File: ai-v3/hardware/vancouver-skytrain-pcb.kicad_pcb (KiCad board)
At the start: 2 copper layers, 150 x 150 mm, 85 parts, among them SW1 TS-1187A-B-A-B, SW2 TS-1187A-B-A-B, SW3 TS-1187A-B-A-B, SW4 TS-1187A-B-A-B, U1 XIAO-RP2040-DIP

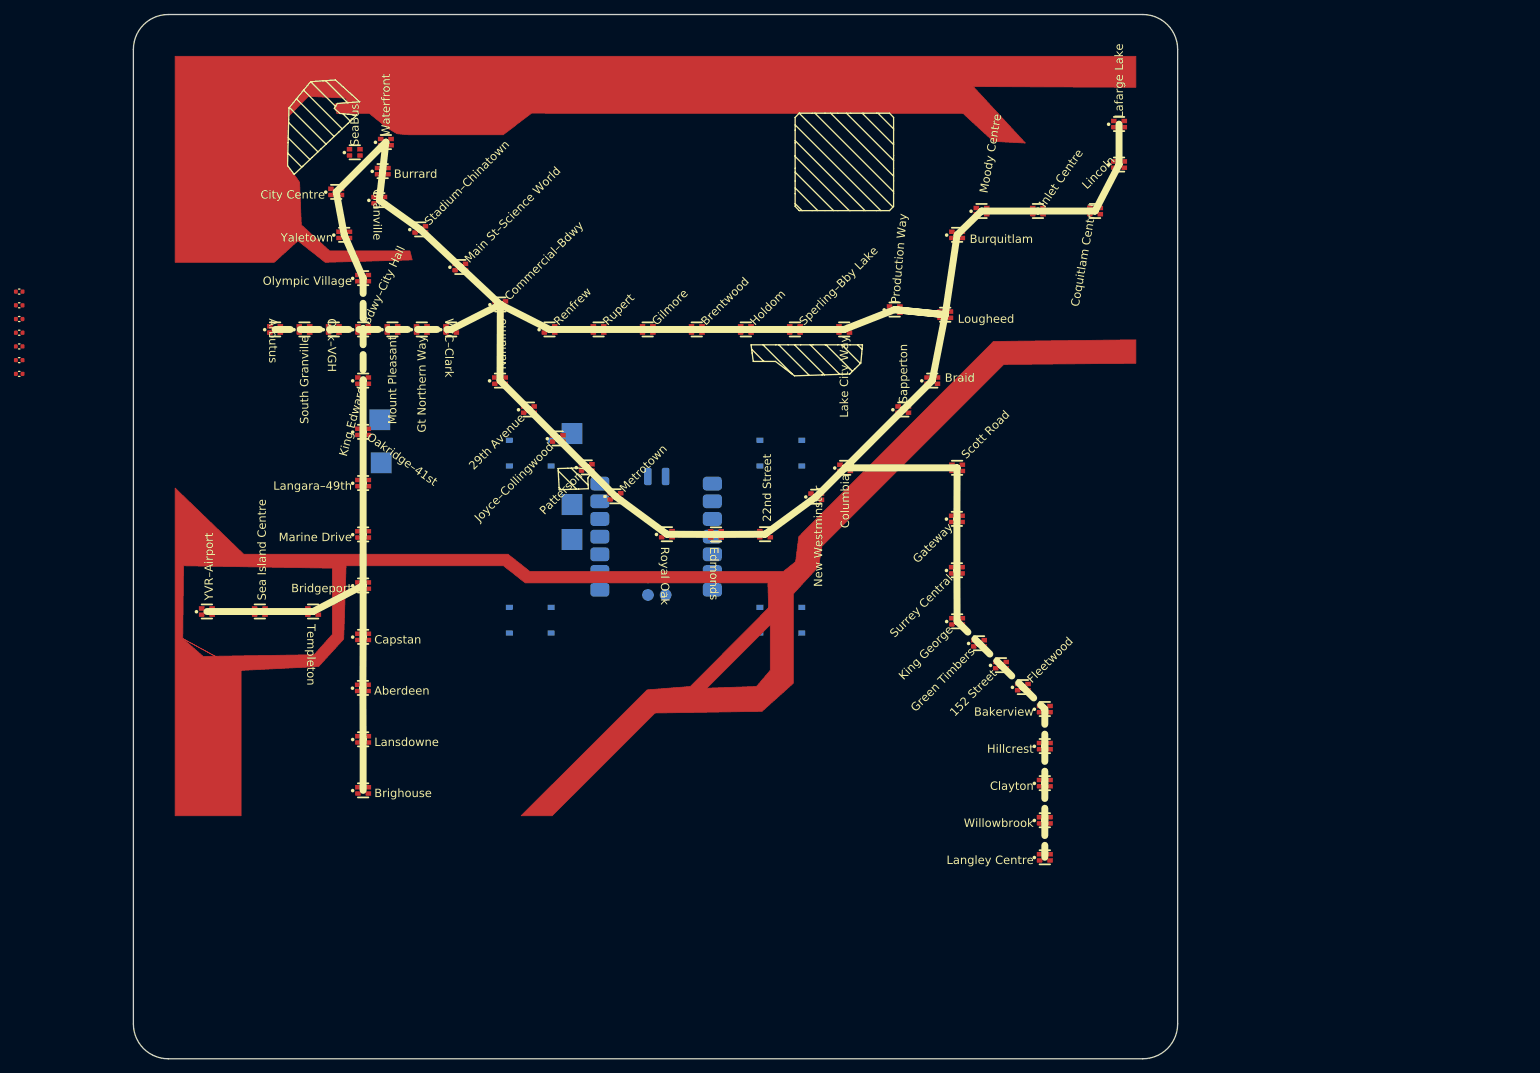
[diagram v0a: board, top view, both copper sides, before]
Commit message: ai-v3: design-review pass - west coast, Delta, wordmark, readable labels
Left edge now ends in water: build_geo.py carves the Point Grey tip out
of the traced land in the PDF's own 45-degree idiom (the source draws no
coastline west of Cambie; v2's look came from a wider frame, not from
data), and the frame extends below the page so Delta / the South Arm /
Boundary Bay fill the bottom third instead of blank soldermask.

Map furniture: exposed-copper VANCOUVER wordmark (v2 style), 49th
parallel dash-dot border with CANADA/USA, legend (existing / future /
SeaBus), SeaBus dotted ferry route. New "line" geo type and "copper"
annotations in export_art.

Labels: 0.15 mm stroke, 1.9 mm standoff from the LED, two-line wrapping
of long names (no more Bdwy/Bby abbreviations), leader hairlines for
stations with no clean spot beside the pad. auto_label rewritten to
score per station (check_fit.Context fast path, 10 s instead of hours),
prefer one angle per corridor, and check labels against their own route
segment beyond the standoff. Routes 1.5 mm; silk station rings, heavier
at interchanges (Columbia, Bridgeport, Production Way now flagged).

Co-Authored-By: Claude Fable 5.1 <noreply@anthropic.com>
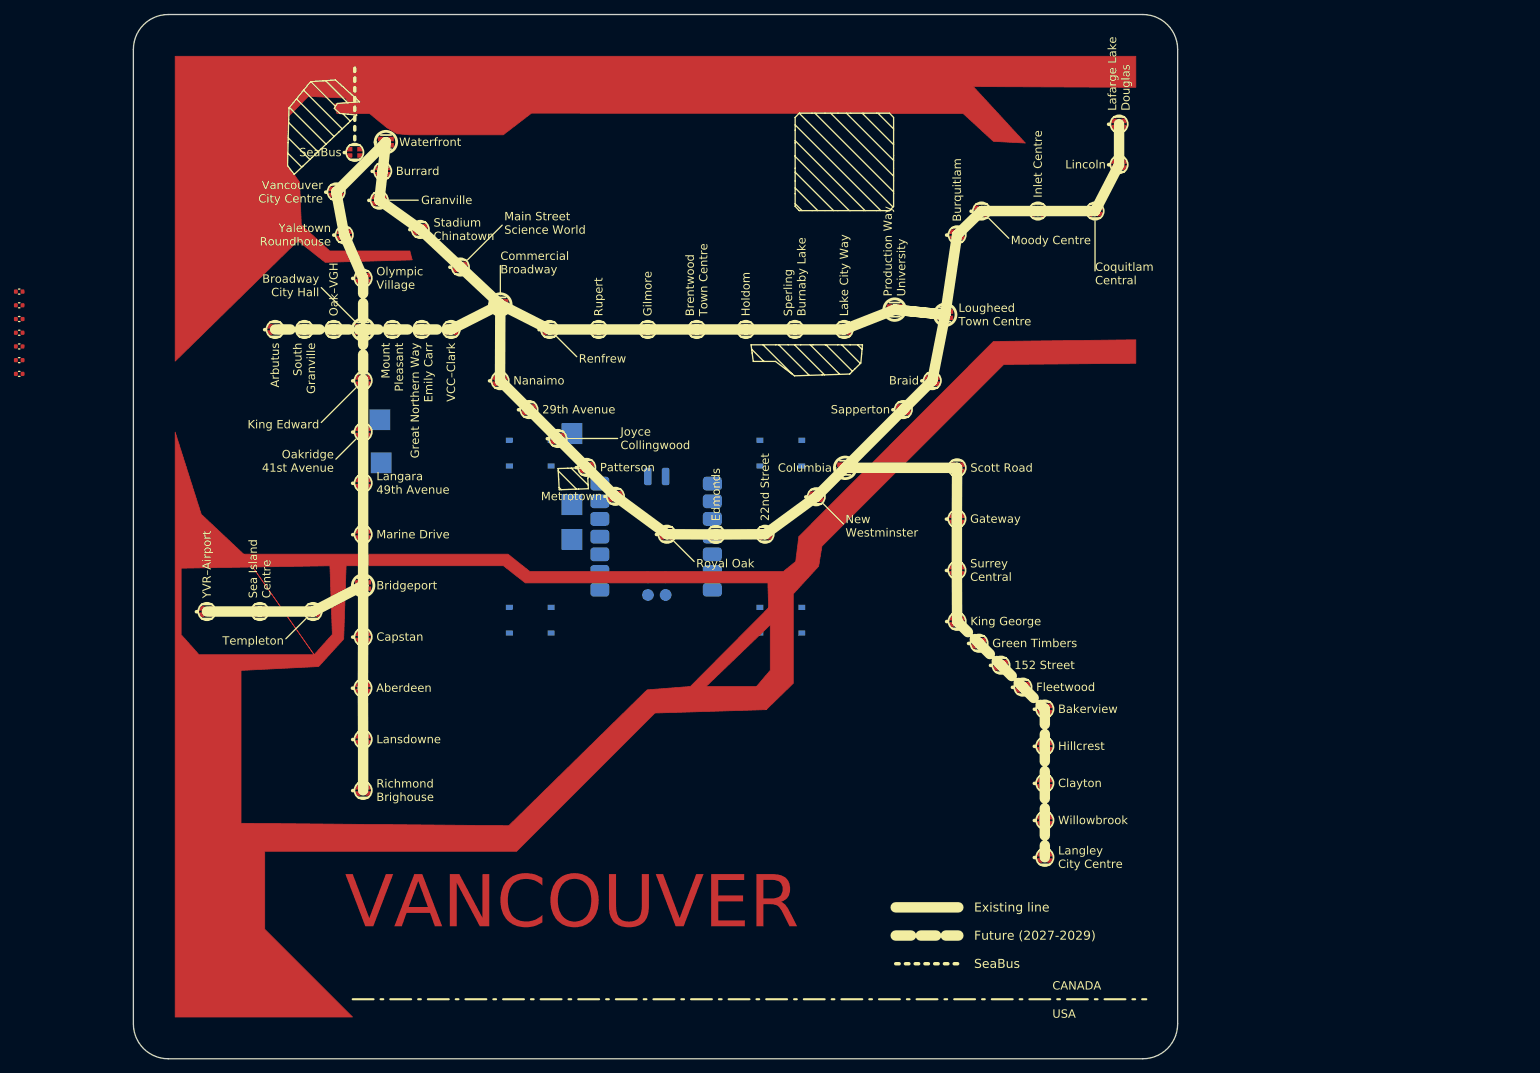
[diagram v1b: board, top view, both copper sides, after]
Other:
- board text added: "Brentwood Town Centre"
- board text added: "Broadway City Hall"
- board text added: "CANADA"
- board text added: "Commercial Broadway"
- board text added: "Existing line"
- board text added: "Future (2027-2029)"
- board text added: "Great Northern Way Emily Carr"
- board text added: "Joyce Collingwood"
- board text added: "Lafarge Lake Douglas"
- board text added: "Langara 49th Avenue"
- board text added: "Langley City Centre"
- board text added: "Lougheed Town Centre"
- board text added: "Main Street Science World"
- board text added: "Oakridge 41st Avenue"
- board text added: "Production Way University"
- board text added: "Richmond Brighouse"
- board text added: "Sperling Burnaby Lake"
- board text added: "Stadium Chinatown"
- board text added: "USA"
- board text added: "VANCOUVER"
- board text added: "Vancouver City Centre"
- board text added: "Vancouver Skytrain Github.com/Funvill/Vancouver-Skytrain-PCB Version: 2026-Sep-05"
- board text added: "Yaletown Roundhouse"
- board text removed: "Bdwy–City Hall"
- board text removed: "Brentwood"
- board text removed: "Brighouse"
- board text removed: "City Centre"
- board text removed: "Commercial–Bdwy"
- board text removed: "Gt Northern Way"
- board text removed: "Joyce–Collingwood"
- board text removed: "Lafarge Lake"
- board text removed: "Langara–49th"
- board text removed: "Langley Centre"
- board text removed: "Lougheed"
- board text removed: "Main St–Science World"
- board text removed: "Oakridge–41st"
- board text removed: "Production Way"
- board text removed: "Sperling–Bby Lake"
- board text removed: "Stadium–Chinatown"
- board text removed: "Vancouver Skytrain Github.com/Funvill/Vancouver-Skytrain-PCB Version: 2026-Aug-31"
- board text removed: "Yaletown"

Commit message: ai-v3: switch station layout and geography to the v1 natural map
The TransLink schematic's 1.26:1 page stretched everything south of
Broadway and turned the Fraser into a 45-degree band. Replace it with
v1's natural-geography map (v1/input/natrual/map.svg): real coastline -
Burrard Inlet with the North Shore, Point Grey, the Fraser's arms,
Boundary Bay - and v1's station layout drawn over it.

input/build_from_v1.py: stations = midpoints of v1's N/S LED pairs,
mapped from the v1 board into the map's frame by a similarity fit
(v1 rotated the map ~9 deg; we keep the map's orientation) and snapped
to map.png's station dots where one is within 2.5 mm. Coastline parsed
from the SVG (parse_v1_coast.py) and assembled even-odd so islands are
holes; the Fraser is carried east to the frame for Langley. One uniform
scale, full width. Surrey-Langley from lat/lon at the map's east-west
scale with the southward slope capped to stay on the page; Capstan and
SeaBus (Lonsdale Quay, as v1 had it) placed by hand.

Copper safety with a real coastline: a 2.4 mm clearance disk carved out
of the water around every LED (several now sit in water), chain pushes
plus a global pairwise separation for the 2.8 mm pitch; DRC has no
clearance/shorting violations. test_vancouver_data now measures pitch in
board mm. Labels 1.1 mm; tight corridors single-line; leaders penalised
harder; furniture band follows the map bottom.

Co-Authored-By: Claude Fable 5.1 <noreply@anthropic.com>
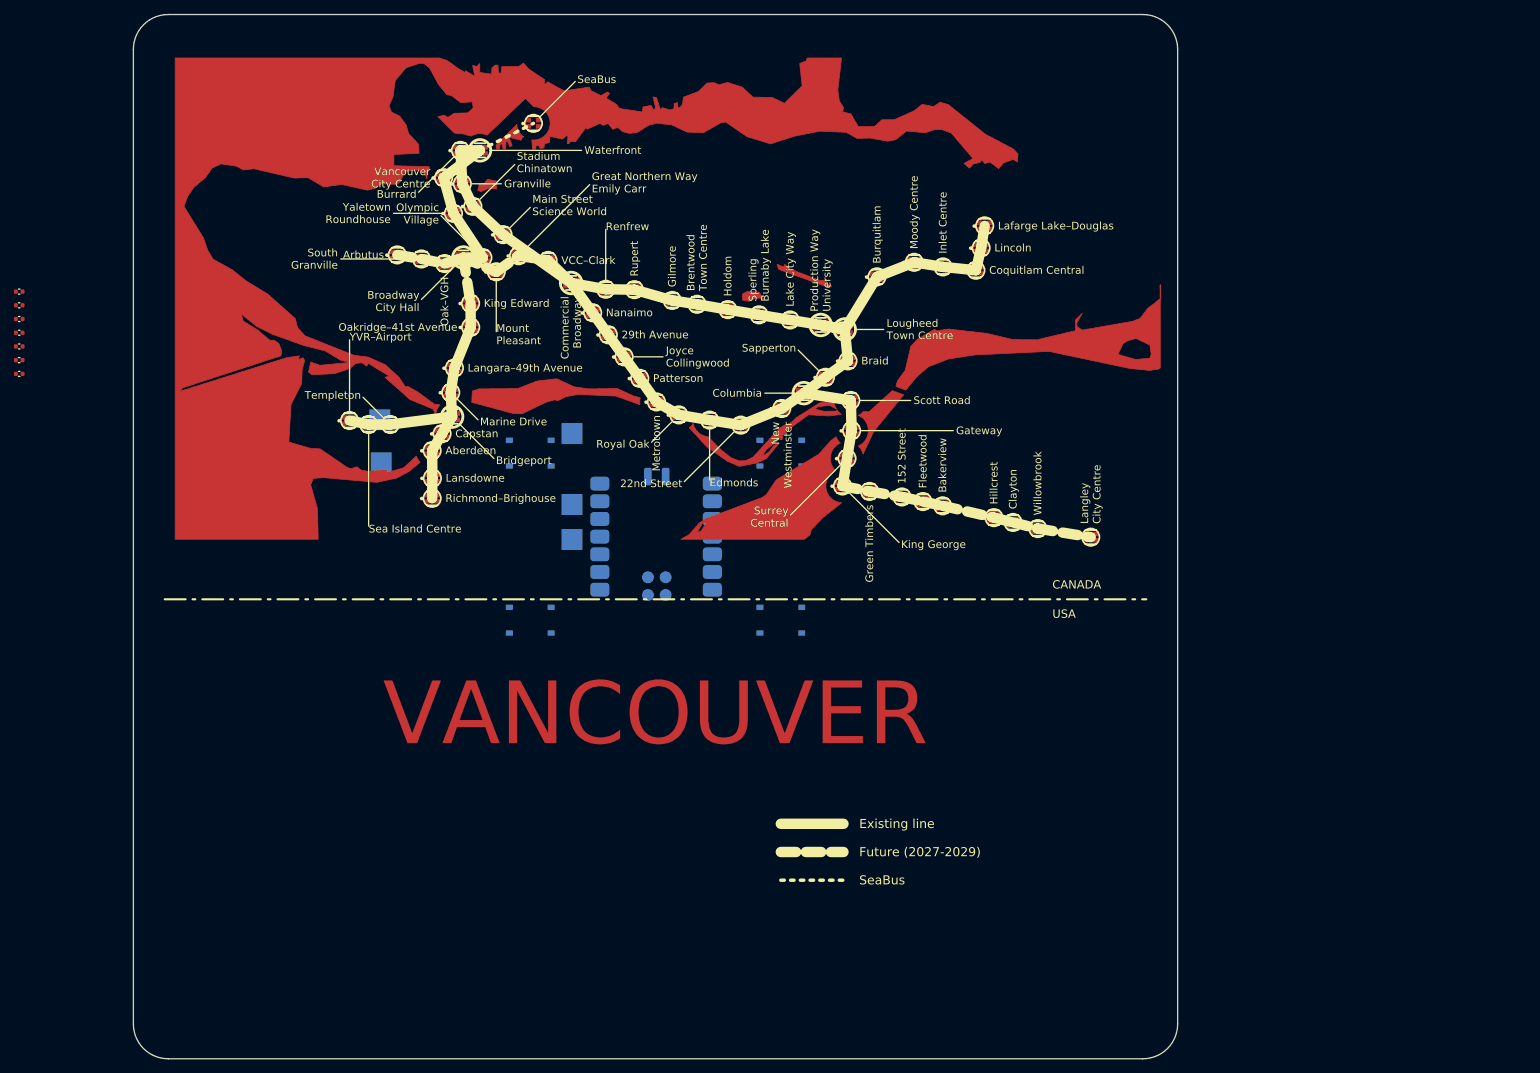
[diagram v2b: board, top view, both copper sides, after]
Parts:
- moved LED29 46.5 mm to (137.5, 75.1)
- moved LED68 43.1 mm to (42.9, 69.5)
- moved LED28 41.9 mm to (129.9, 73.8)
- moved LED67 38.8 mm to (42.9, 66.6)
- moved LED27 37.7 mm to (126.4, 73.0)
- moved LED66 35.5 mm to (42.9, 62.6)
- moved LED64 34.2 mm to (31.1, 58.3)
- moved LED26 33.6 mm to (123.6, 72.3)
- moved LED25 32.7 mm to (116.2, 70.6)
- moved LED65 31.3 mm to (44.3, 60.2)
- moved LED63 31.1 mm to (33.8, 58.9)
- moved LED24 30.3 mm to (113.4, 70.0)
- moved LED62 29.1 mm to (36.9, 58.9)
- moved LED23 28.0 mm to (110.4, 69.3)
- moved LED61 27.4 mm to (45.8, 57.8)
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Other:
- board text added: "Lafarge Lake–Douglas"
- board text added: "Langara–49th Avenue"
- board text added: "Oakridge–41st Avenue"
- board text added: "Richmond–Brighouse"
- board text added: "Vancouver Skytrain Github.com/Funvill/Vancouver-Skytrain-PCB Version: 2026-Sep-06"
- board text removed: "Lafarge Lake Douglas"
- board text removed: "Langara 49th Avenue"
- board text removed: "Oakridge 41st Avenue"
- board text removed: "Richmond Brighouse"
- board text removed: "Vancouver Skytrain Github.com/Funvill/Vancouver-Skytrain-PCB Version: 2026-Sep-05"

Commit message: ai-v3: rebuild from OpenStreetMap - real shoreline, 150x86 board
Station positions and geography now come from OSM (input/build_from_osm.py,
Overpass responses cached in input/osm/): real station nodes; sea/inlet/
Fraser arms from natural=coastline ways (land-on-the-left rule over
polygonized faces); the Fraser main stem and Pitt River as buffered
centrelines where the coastline stops; only the large named lakes
(Burnaby, Deer, Trout, Como, Lost Lagoon...). Shoreline smoothed with a
morphological open/close + simplify, small river islands filled, edge
slivers dropped.

Board is the frame's own aspect, 150 x 86.2 mm (canvas_h_mm, non-square
support through citymap/check_fit/render_map/reposition_board); water
runs to the board edge with a 0.4 mm copper clearance and corner-aware
clamping - no border. Wordmark placed on land (Delta) clear of water and
track; legend and border removed. Routes one solid 1.0 mm style.

Labels: zero collisions, including new leader-vs-label and
leader-vs-leader checks; more leader directions/rings and a first-part-
of-name fallback for the Broadway corridor. LED pitch floor raised to
3.3 mm (diagonal neighbours' pads at 2.8 mm violated clearance); river-
bank stations nudged onto land, SeaBus on the North Shore at Lonsdale
Quay. DRC: no clearance / edge / shorting violations.

Co-Authored-By: Claude Fable 5.1 <noreply@anthropic.com>
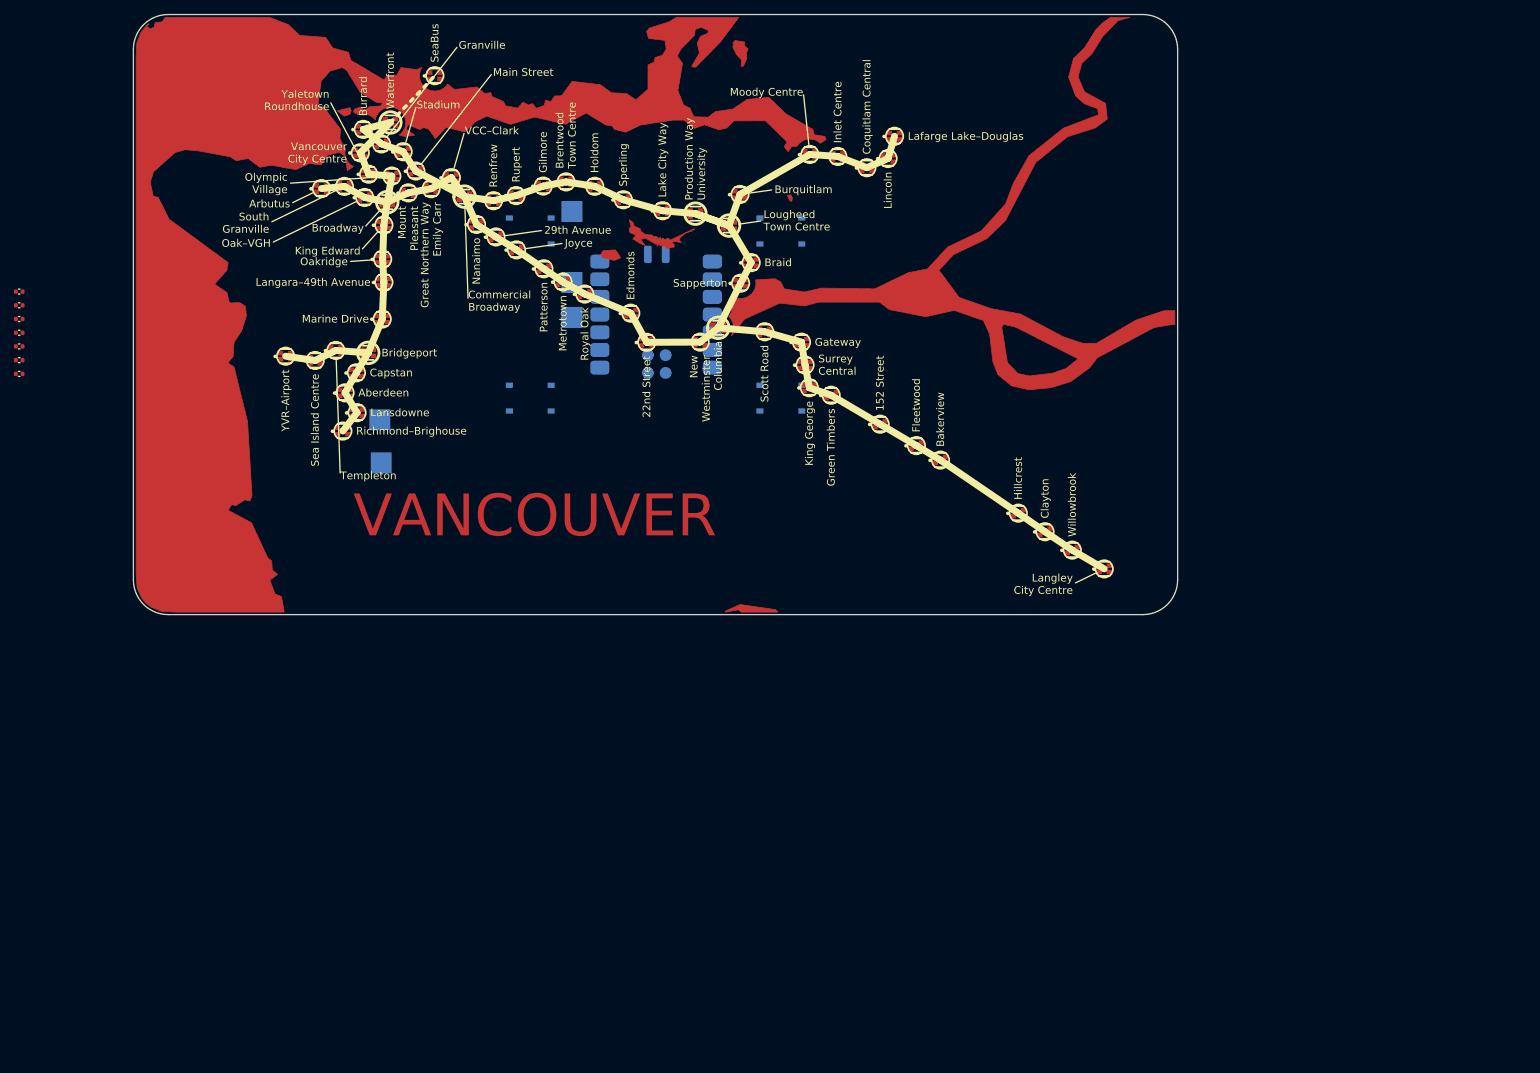
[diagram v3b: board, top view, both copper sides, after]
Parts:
- moved +5V 31.9 mm to (63.0, 43.5)
- moved GND 31.9 mm to (63.0, 38.5)
- moved LED_IN 31.9 mm to (63.0, 28.3)
- moved SW1 31.9 mm to (57.0, 31.1)
- moved SW2 31.9 mm to (57.0, 55.1)
- moved SW3 31.9 mm to (93.0, 31.1)
- moved SW4 31.9 mm to (93.0, 55.1)
- moved U1 31.9 mm to (75.0, 43.1)
- moved LED42 26.1 mm to (66.3, 24.7)
- moved LED43 25.8 mm to (62.1, 24.0)
- moved LED41 25.6 mm to (70.4, 26.6)
- moved LED44 24.8 mm to (58.9, 24.6)
- moved LED40 24.1 mm to (76.0, 28.2)
- moved LED33 24.1 mm to (80.7, 28.6)
- moved LED34 23.0 mm to (87.1, 25.8)
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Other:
- board size 150 x 150 mm -> 150 x 86.2 mm
- board text added: "Broadway"
- board text added: "Joyce"
- board text added: "Main Street"
- board text added: "Oakridge"
- board text added: "Sperling"
- board text added: "Stadium"
- board text added: "Vancouver Skytrain Github.com/Funvill/Vancouver-Skytrain-PCB Version: 2026-Sep-06b"
- board text removed: "Broadway City Hall"
- board text removed: "CANADA"
- board text removed: "Existing line"
- board text removed: "Future (2027-2029)"
- board text removed: "Joyce Collingwood"
- board text removed: "Main Street Science World"
- board text removed: "Oakridge–41st Avenue"
- board text removed: "Sperling Burnaby Lake"
- board text removed: "Stadium Chinatown"
- board text removed: "USA"
- board text removed: "Vancouver Skytrain Github.com/Funvill/Vancouver-Skytrain-PCB Version: 2026-Sep-06"
